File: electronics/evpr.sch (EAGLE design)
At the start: 115 parts, among them J1 10118193-0001LF, J2 B4P-VH(LF)(SN), Q1 AOD4184A, Q2 AOD4184A, T3 MMBT2222A, T5 MMBT2222A, U2 BQ2057TTS, U3 ESP32-WROOM-32D, U6 SN74AHCT125DR, U7 TPSM84824MOLR, U8 LTC4353CMSPBFMSOP-16_MS-M, X1 B3P-VH(LF)(SN), X2 B3P-VH(LF)(SN), X3 B3P-VH(LF)(SN)

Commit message: Altered Battery Charge Symbol and cleaned up battery charge schematic
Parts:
- removed U2: BQ2057TTS, BQ2057TTS:BQ2057TTS
- added U1: BQ2057TTS, mccloud:BQ2057TTS
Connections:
- removed net N$2: R4.1, U2.CC
- new net N$9: R4.1, U1.CC
- net CSTAT: now also U1.STAT; no longer U2.STAT
- net GND: now also U1.VSS; no longer U2.VSS
- net N$5: now also U1.SNS; no longer U2.SNS
- net N$7: now also U1.TS; no longer U2.TS
- net VBAT: now also U1.BAT; no longer U2.BAT
- net VRAW: now also U1.COMP, U1.VCC; no longer U2.COMP, U2.VCC
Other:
- moved on the sheet: C13, C16, C22, C23, C24, LED2, R12, R13, R14, R16, R3, R4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

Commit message: Replaced R31 and R2 with R8 and R32 respectively, 0603 outline and corrected part selection.
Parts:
- removed R2: 768Ω 1%, rcl:R-US_R0805
- removed R31: 37.4kΩ 1%, rcl:R-US_R0805
- added R11: 768Ω 1%, rcl:R-US_R0603
- added R8: 37.4kΩ 1%, rcl:R-US_R0603
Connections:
- net AGND: now also R11.1, R8.1; no longer R2.2, R31.2
- net N$17: now also R8.2; no longer R31.1
- net N$3: now also R11.2; no longer R2.1
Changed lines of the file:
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@@
 <attribute name="COMPONENT" value="PTN0805E1002BST1"/>
-</part>
-<part name="R2" library="rcl" deviceset="R-US_" device="R0805" value="768Ω 1%">
-<attribute name="COMPONENT" value="RC0402FR-07768RL"/>
-</part>
-<part name="R31" library="rcl" deviceset="R-US_" device="R0805" value="37.4kΩ 1%">
-<attribute name="COMPONENT" value="RC0201FR-0737K4L"/>
 </part>
 <part name="C1" library="mccloud" deviceset="C3225X7R1E106K250AC" device="" value="10µF">
@@
 <part name="SUPPLY8" library="supply2" library_urn="urn:adsk.eagle:library:372" deviceset="GND" device=""/>
 <part name="SUPPLY12" library="supply2" library_urn="urn:adsk.eagle:library:372" deviceset="GND" device=""/>
+<part name="R8" library="rcl" library_urn="urn:adsk.eagle:library:334" deviceset="R-US_" device="R0603" package3d_urn="urn:adsk.eagle:package:23555/3" value="37.4kΩ 1%">
+<spice>
+<pinmapping spiceprefix="R">
+<pinmap gate="G$1" pin="1" pinorder="1"/>
+<pinmap gate="G$1" pin="2" pinorder="2"/>
+</pinmapping>
+</spice>
+<attribute name="COMPONENT" value="RC0603FR-0737K4L"/>
+</part>
+<part name="R11" library="rcl" library_urn="urn:adsk.eagle:library:334" deviceset="R-US_" device="R0603" package3d_urn="urn:adsk.eagle:package:23555/3" value="768Ω 1%">
+<spice>
+<pinmapping spiceprefix="R">
+<pinmap gate="G$1" pin="1" pinorder="1"/>
+<pinmap gate="G$1" pin="2" pinorder="2"/>
+</pinmapping>
+</spice>
+<attribute name="COMPONENT" value="RMCF0603FT768R"/>
+</part>
 </parts>
 <sheets>
@@
 <attribute name="COMPONENT" x="-73.66" y="-25.4" size="1.778" layer="96" display="off"/>
 </instance>
-<instance part="R2" gate="G$1" x="-73.66" y="-46.99" smashed="yes" rot="R270">
-<attribute name="NAME" x="-71.12" y="-46.7614" size="1.778" layer="95"/>
-<attribute name="VALUE" x="-71.12" y="-49.022" size="1.778" layer="96"/>
-<attribute name="COMPONENT" x="-73.66" y="-46.99" size="1.778" layer="96" display="off"/>
-</instance>
-<instance part="R31" gate="G$1" x="-147.32" y="-50.8" smashed="yes" rot="R270">
-<attribute name="NAME" x="-149.86" y="-48.26" size="1.778" layer="95" rot="R180"/>
-<attribute name="VALUE" x="-149.86" y="-50.8" size="1.778" layer="96" rot="R180"/>
-<attribute name="COMPONENT" x="-147.32" y="-50.8" size="1.778" layer="96" display="off"/>
-</instance>
 <instance part="C1" gate="G$1" x="-193.04" y="-20.32" smashed="yes" rot="R90">
 <attribute name="VALUE" x="-194.31" y="-24.13" size="1.78071875" layer="96" ratio="10" rot="SR180"/>
@@
 <instance part="SUPPLY12" gate="GND" x="-129.54" y="22.86" smashed="yes">
 <attribute name="VALUE" x="-128.27" y="25.4" size="1.778" layer="96"/>
+</instance>
+<instance part="R8" gate="G$1" x="-147.32" y="-50.8" smashed="yes" rot="R90">
+<attribute name="NAME" x="-151.3586" y="-54.61" size="1.778" layer="95" rot="R90"/>
+<attribute name="VALUE" x="-148.59" y="-54.61" size="1.778" layer="96" rot="R90"/>
+<attribute name="COMPONENT" x="-147.32" y="-50.8" size="1.778" layer="96" rot="R90" display="off"/>
+</instance>
+<instance part="R11" gate="G$1" x="-73.66" y="-48.26" smashed="yes" rot="R90">
+<attribute name="NAME" x="-77.6986" y="-52.07" size="1.778" layer="95" rot="R90"/>
+<attribute name="VALUE" x="-74.93" y="-52.07" size="1.778" layer="96" rot="R90"/>
+<attribute name="COMPONENT" x="-73.66" y="-48.26" size="1.778" layer="96" rot="R90" display="off"/>
 </instance>
 </instances>
@@
 <segment>
 <pinref part="R1" gate="G$1" pin="2"/>
-<pinref part="R2" gate="G$1" pin="1"/>
 <wire x1="-73.66" y1="-30.48" x2="-73.66" y2="-35.56" width="0.1524" layer="91"/>
 <pinref part="U7" gate="A" pin="FB"/>
-<wire x1="-73.66" y1="-35.56" x2="-73.66" y2="-41.91" width="0.1524" layer="91"/>
 <wire x1="-93.98" y1="-35.56" x2="-73.66" y2="-35.56" width="0.1524" layer="91"/>
+<pinref part="R11" gate="G$1" pin="2"/>
+<wire x1="-73.66" y1="-43.18" x2="-73.66" y2="-35.56" width="0.1524" layer="91"/>
 <junction x="-73.66" y="-35.56"/>
 </segment>
@@
 <segment>
 <pinref part="U7" gate="A" pin="RT_CLK"/>
-<pinref part="R31" gate="G$1" pin="1"/>
 <wire x1="-139.7" y1="-45.72" x2="-147.32" y2="-45.72" width="0.1524" layer="91"/>
+<pinref part="R8" gate="G$1" pin="2"/>
 </segment>
 </net>
@@
 <net name="AGND" class="0">
 <segment>
-<pinref part="R2" gate="G$1" pin="2"/>
-<pinref part="R31" gate="G$1" pin="2"/>
-<wire x1="-73.66" y1="-60.96" x2="-73.66" y2="-52.07" width="0.1524" layer="91"/>
 <wire x1="-147.32" y1="-60.96" x2="-147.32" y2="-55.88" width="0.1524" layer="91"/>
 <pinref part="U7" gate="A" pin="AGND"/>
@@
 <wire x1="-78.74" y1="-63.5" x2="-78.74" y2="-60.96" width="0.1524" layer="91"/>
 <junction x="-78.74" y="-60.96"/>
-</segment>
-</net>
+<pinref part="R8" gate="G$1" pin="1"/>
+<pinref part="R11" gate="G$1" pin="1"/>
+<wire x1="-73.66" y1="-60.96" x2="-73.66" y2="-53.34" width="0.1524" layer="91"/>
+</segment>
+</net>

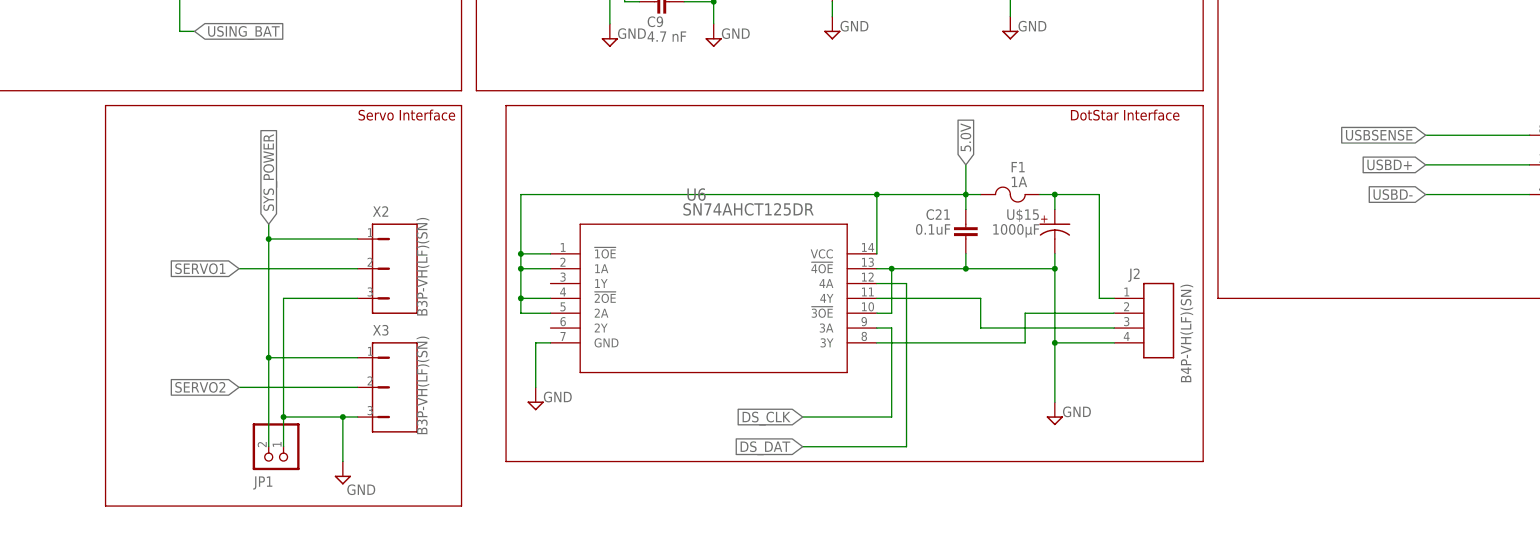
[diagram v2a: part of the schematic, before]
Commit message: Replaced Dot-Star, Servo, PAD connectors with new JST-PA SMD connectors, saving significant board space.
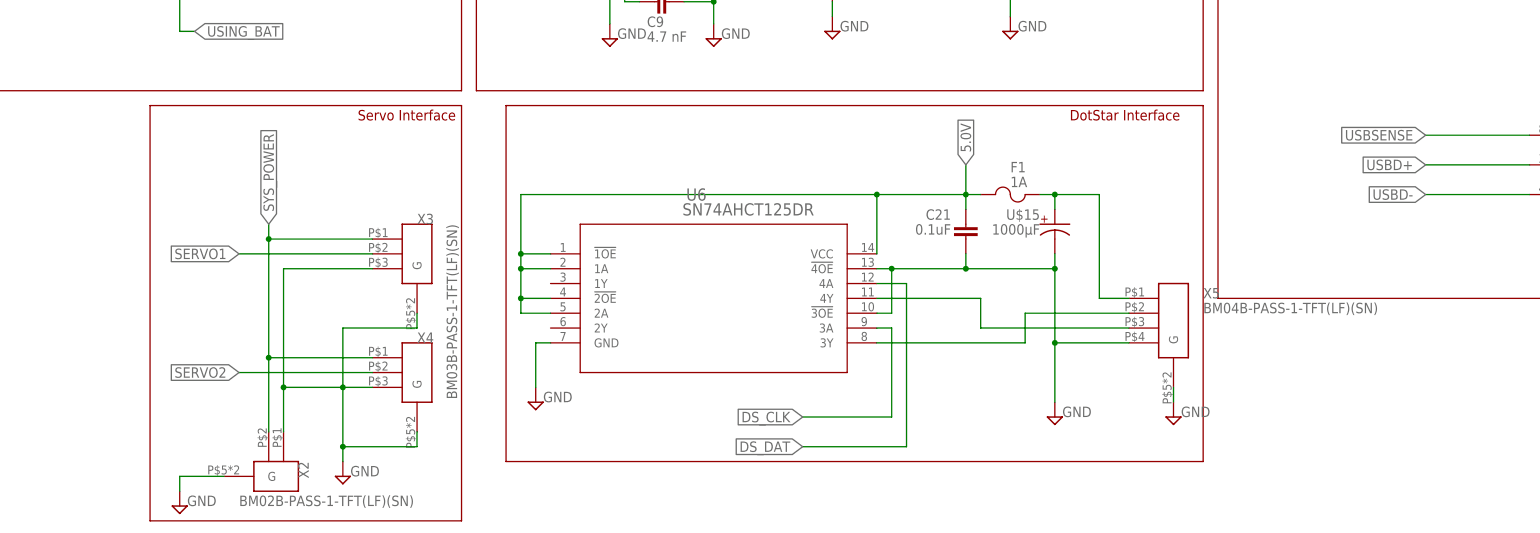
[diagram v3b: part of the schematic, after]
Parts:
- removed J2: B4P-VH(LF)(SN), mccloud:B4P-VH(LF)(SN)
- removed JP1: (no value), pinhead:PINHD-1X2/90
- added X4: BM03B-PASS-1-TFT(LF)(SN), mccloud:BM03B-PASS-1-TFT(LF)(SN)
- added X5: BM04B-PASS-1-TFT(LF)(SN), mccloud:BM04B-PASS-1-TFT(LF)(SN)
- X2: value B3P-VH(LF)(SN) -> BM02B-PASS-1-TFT(LF)(SN); device B3P-VH_LF__SN_:B3P-VH(LF)(SN) -> mccloud:BM02B-PASS-1-TFT(LF)(SN); COMPONENT B3P-VH(LF)(SN) -> (none)
- X3: value B3P-VH(LF)(SN) -> BM03B-PASS-1-TFT(LF)(SN); device B3P-VH_LF__SN_:B3P-VH(LF)(SN) -> mccloud:BM03B-PASS-1-TFT(LF)(SN); COMPONENT B3P-VH(LF)(SN) -> (none)
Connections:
- net GND: now also X2.1, X2.G, X3.G, X4.3, X4.G, X5.4, X5.G; no longer J2.4, JP1.1, X2.3
- net N$22: now also X5.3; no longer J2.3
- net N$27: now also X5.2; no longer J2.2
- net N$28: now also X5.1; no longer J2.1
- net SERVO1: now also X3.2; no longer X2.2
- net SERVO2: now also X4.2; no longer X3.2
- net SYS_POWER: now also X2.2, X4.1; no longer JP1.2, X2.1
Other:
- moved on the sheet: X3

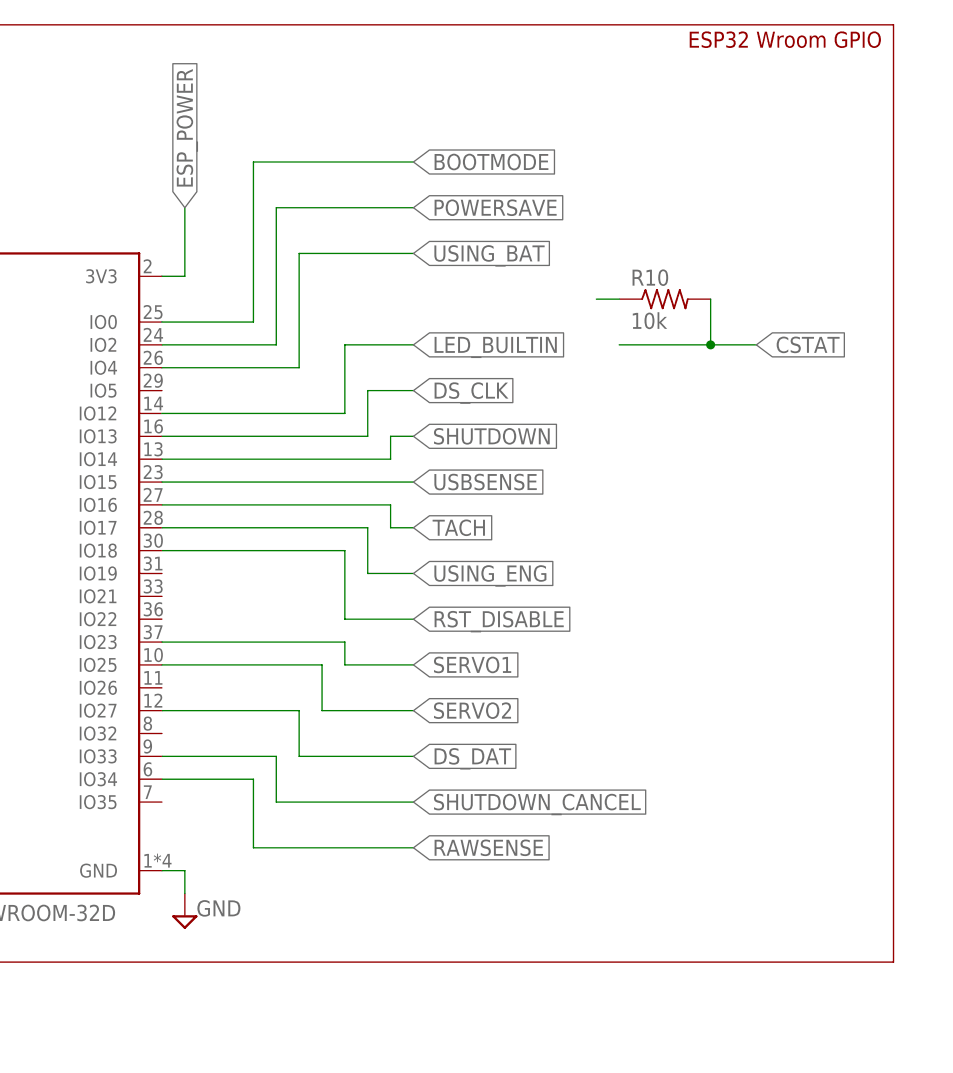
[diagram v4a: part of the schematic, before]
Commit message: Rerouted CSTAT pins
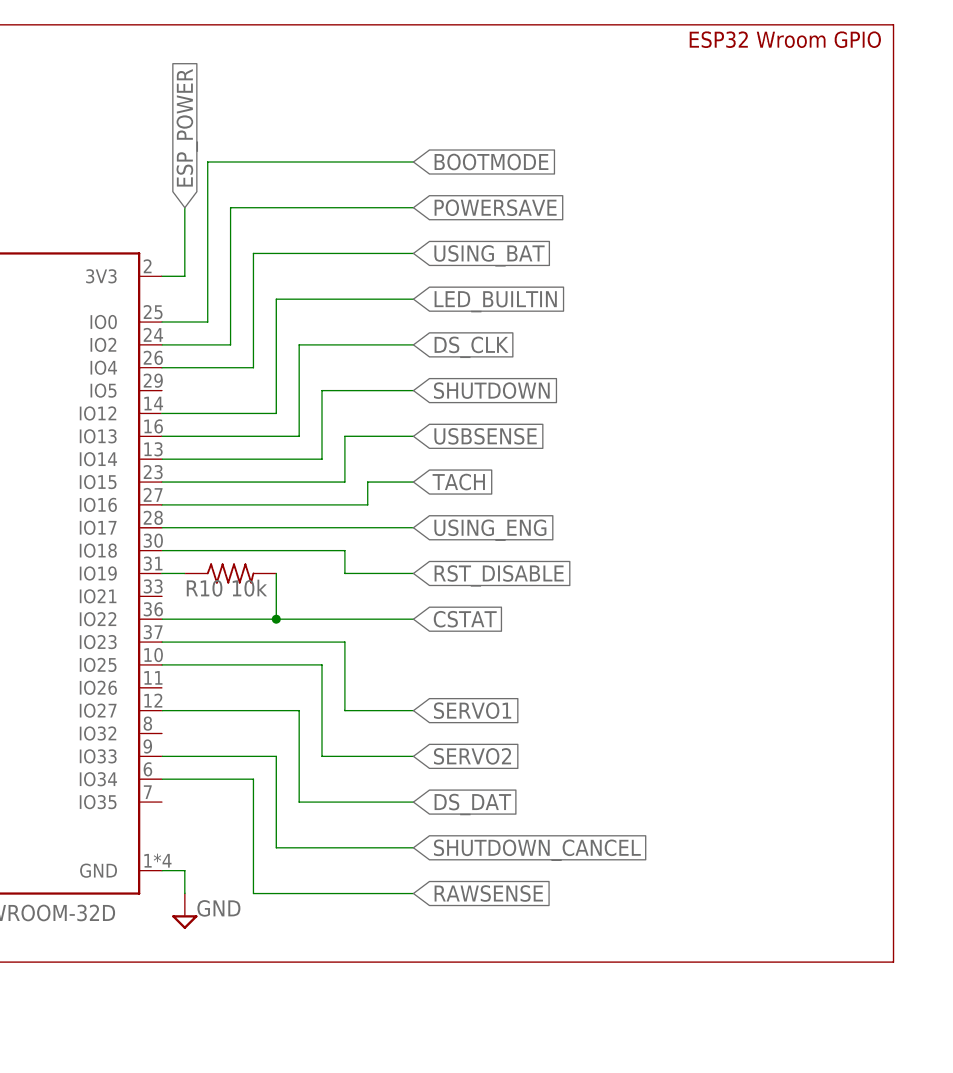
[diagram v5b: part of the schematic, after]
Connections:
- removed net N$47: R10.1
- new net N$2: R10.1, U3.IO19
- net CSTAT: now also U3.IO22
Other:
- moved on the sheet: R10

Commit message: Replace passives with 0603 wherever possible.
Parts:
- added C27, C28, C29, C30, C31, C32, C33, C34, C35, C36, C37, C38: 0.1uF, eagle-ltspice:CC0603
- C11: COMPONENT CL32A226MOJNNNE -> CL10A226MO7JZNC
- C14, C17: device eagle-ltspice:CC1210 -> rcl:C-USC0603; COMPONENT C1210C106M4PACTU -> GRM188R61A106KE69D
- C15, C19, C20: device eagle-ltspice:CC1210 -> rcl:C-USC0603; COMPONENT CL32A226MOJNNNE -> CL10A226MO7JZNC
- R1: device rcl:R-US_R0805 -> rcl:R-US_R0603; COMPONENT PTN0805E1002BST1 -> RG1608P-103-B-T5
- R10, R13, R14, R28, R7, R9: device rcl:R-US_R0805 -> rcl:R-US_R0603; COMPONENT CR0805-JW-103ELF -> RMCF0603FT10K0
- R11: value 768Ω 1% -> 768Ω 0.1%; COMPONENT RMCF0603FT768R -> RQ73C1J768RBTD
- R12, R4: device rcl:R-US_R0805 -> rcl:R-US_R0603; COMPONENT RC0805JR-071KL -> RMCF0603FT1K00
- R15: device rcl:R-US_R0805W -> rcl:R-US_R0603; COMPONENT CRCW0805499RFKEAHP -> RMCF0603FT1K00
- R16, R17: device rcl:R-US_R0805W -> rcl:R-US_R0603; COMPONENT CRCW0805249RFKEAHP -> RMCF0603JT300R
- R18, R21, R23, R25, R27: device rcl:R-US_R0805W -> rcl:R-US_R0603; COMPONENT RNCP0805FTD22K1 -> RMCF0603FT22K1
- R19, R24, R26: device rcl:R-US_R0805W -> rcl:R-US_R0603; COMPONENT RC0805FR-0747K5L -> RMCF0603FT47K5
- R20: device rcl:R-US_R0805W -> rcl:R-US_R0603; COMPONENT (none) -> RMCF0603FT100K
- R22: device rcl:R-US_R0805W -> rcl:R-US_R0603; COMPONENT RC0805FR-07100KL -> RMCF0603FT100K
- R30: device rcl:R-US_R0805W -> rcl:R-US_R0603; COMPONENT RC0805FR-071ML -> RMCF0603FG1M00
- R32: device rcl:R-US_R0805 -> rcl:R-US_R0603; COMPONENT RC0805FR-0795K3L -> RMCF0603FT95K3
- R33, R34, R5, R6: device rcl:R-US_R0805 -> rcl:R-US_R0603; COMPONENT RC0805FR-07100KL -> RMCF0603FT100K
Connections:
- net 5.0V: now also C36.2
- net ESP_POWER: now also C34.2
- net GND: now also C27.2, C28.2, C29.1, C30.2, C31.2, C32.2, C33.2, C34.1, C35.1, C36.1, C37.1, C38.1
- net N$51: now also C35.2
- net N$8: now also C31.1
- net SYS_POWER: now also C33.1, C37.2, C38.2
- net TACH_RAW: now also C27.1
- net VBAT: now also C30.1, C32.1
- net VCONV: now also C29.2
- net VRAW: now also C28.1
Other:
- moved on the sheet: C1, C13, C19, R3, R4, R5, R6, TP12, TP6, U$3, U1, X1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

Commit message: Added EMI Testing optionals
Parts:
- added C39, C40, EC1, EC2, EC3, EC4, EC5: 0.1uF, eagle-ltspice:CC0603
- added ER1, ER2, ER3, ER4: 0, rcl:R-US_R0603
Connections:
- new net N$11: ER1.1, X3.2
- new net N$12: ER2.1, X4.2
- new net N$30: ER3.1, X5.2
- new net N$42: ER4.1, X5.3
- net ESP_POWER: now also C39.2
- net GND: now also C39.1, C40.2, EC1.2, EC2.2, EC3.2, EC4.2, EC5.2
- net N$22: now also EC4.1, ER4.2; no longer X5.3
- net N$27: now also EC5.1, ER3.2; no longer X5.2
- net SERVO1: now also EC2.1, ER1.2; no longer X3.2
- net SERVO2: now also EC3.1, ER2.2; no longer X4.2
- net TACH: now also EC1.1
- net VRAW: now also C40.1
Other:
- note added: "B: Battery Charge Control"
- note added: "D: DotStar Interface"
- note added: "F: 5V Power Management"
- note added: "G: ESP32 Wroom GPIO"
- note added: "I: Power & Tachometer Interface"
- note added: "L: Battery Interface"
- note added: "M: Engine Power to 8.4V"
- note added: "P: ESP32 USB Serial / Programming Interface"
- note added: "S: Servo Interface"
- note added: "T: ESP32 Reset"
- note added: "Y: SYS_POWER Management"
- note added: "Z: ESP32 / Deep Sleep Power"
- note removed: "5V Power Management"
- note removed: "Battery Charge Control"
- note removed: "Battery Interface"
- note removed: "DotStar Interface"
- note removed: "ESP32 / Deep Sleep Power"
- note removed: "ESP32 Reset"
- note removed: "ESP32 USB Serial / Programming Interface"
- note removed: "ESP32 Wroom GPIO"
- note removed: "Engine Power to 8.4V"
- note removed: "Power & Tachometer Interface"
- note removed: "SYS_POWER Management"
- note removed: "Servo Interface"
- moved on the sheet: C16, C21, C22, C23, C24, C32, C37, C38, F1, LED2, R10, R12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
